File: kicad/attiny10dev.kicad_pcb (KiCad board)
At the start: 2 copper layers, 19 parts, among them J1 Conn_02x06_Odd_Even, J2 Conn_01x06, J3 Conn_01x03_Male, K1 m4-12h, K2 m4-12h, Q1 2N7002, Q2 BSS84, Q3 2N7002, Q4 FZT600, Q5 2N7002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

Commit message: Work on next gen pcb
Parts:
- added C10: 100n, Capacitor_SMD:C_0805_2012Metric_Pad1.15x1.40mm_HandSolder, F.Cu at (239.3, 85.1)
- added C11: 500p, Capacitor_SMD:C_0805_2012Metric_Pad1.15x1.40mm_HandSolder, F.Cu at (259.4, 81.6)
- added C12: 470u, Capacitor_THT:CP_Radial_D8.0mm_P5.00mm, F.Cu at (254.3, 105.8)
- added C4: 1u, Capacitor_SMD:C_0805_2012Metric_Pad1.15x1.40mm_HandSolder, F.Cu at (233.8, 92.5)
- added C5: 100n, Capacitor_SMD:C_0805_2012Metric_Pad1.15x1.40mm_HandSolder, F.Cu at (243.7, 67.6)
- added C6: 100n, Capacitor_SMD:C_0805_2012Metric_Pad1.15x1.40mm_HandSolder, F.Cu at (250.8, 96.8)
- added C7: 100n, Capacitor_SMD:C_0805_2012Metric_Pad1.15x1.40mm_HandSolder, F.Cu at (246.6, 85.2)
- added C8: 100n, Capacitor_SMD:C_0805_2012Metric_Pad1.15x1.40mm_HandSolder, F.Cu at (237.6, 101.1)
- added C9: 470u, Capacitor_THT:CP_Radial_D8.0mm_P5.00mm, F.Cu at (263.6, 105.8)
- added D2: D, Diode_SMD:D_3220_8050Metric_Pad2.65x5.15mm_HandSolder, F.Cu at (259.5, 89.8)
- added F1: 500ma, Fuse:Fuse_1206_3216Metric_Pad1.42x1.75mm_HandSolder, F.Cu at (231.2, 95.9)
- added L1: 33u, Inductor_THT:L_Toroid_Vertical_L13.0mm_W6.5mm_P5.60mm, F.Cu at (272.8, 91.5)
- added R10: 10k, Capacitor_SMD:C_0603_1608Metric_Pad1.05x0.95mm_HandSolder, F.Cu at (254.2, 97.8)
- added R4: 10k, Capacitor_SMD:C_0603_1608Metric_Pad1.05x0.95mm_HandSolder, F.Cu at (217.7, 105.5)
- added R5: 22, Capacitor_SMD:C_0603_1608Metric_Pad1.05x0.95mm_HandSolder, F.Cu at (229.6, 90.7)
- added R6: 22, Capacitor_SMD:C_0603_1608Metric_Pad1.05x0.95mm_HandSolder, F.Cu at (229.6, 89.0)
- added R7: 470m, Resistor_THT:R_Axial_DIN0204_L3.6mm_D1.6mm_P2.54mm_Vertical, F.Cu at (258.3, 97.6)
- added R8: 180, Capacitor_SMD:C_0603_1608Metric_Pad1.05x0.95mm_HandSolder, F.Cu at (263.8, 98.6)
- added R9: 86k, Capacitor_SMD:C_0603_1608Metric_Pad1.05x0.95mm_HandSolder, F.Cu at (256.0, 97.8)
- added SW1: SW_Push, Button_Switch_THT:SW_PUSH_6mm, F.Cu at (220.2, 101.5)
- added U3: ATmega32U4-AU, Package_QFP:TQFP-44_10x10mm_P0.8mm, F.Cu at (243.0, 93.0)
- added U4: MC34063AD, Package_DIP:DIP-8_W10.16mm, F.Cu at (263.3, 84.7)
- added Y1: 16Mhz, Crystal:Crystal_SMD_HC49-SD, F.Cu at (242.9, 104.9)
- C2, C3: value 22u -> 22p; footprint Capacitor_THT:CP_Radial_D12.5mm_P5.00mm -> Capacitor_SMD:C_0805_2012Metric_Pad1.15x1.40mm_HandSolder; moved to F.Cu
- D1, J1, K1, K2, U2: moved to F.Cu
- J2: value Conn_01x06 -> Conn_02x03_Odd_Even; footprint Connector_PinHeader_2.54mm:PinHeader_1x06_P2.54mm_Vertical -> Connector_PinHeader_2.54mm:PinHeader_2x03_P2.54mm_Vertical; moved to F.Cu
- J3: value Conn_01x03_Male -> USB_B; footprint TerminalBlock_RND:TerminalBlock_RND_205-00277_1x03_P5.00mm_Vertical -> Connector_USB:USB_B_OST_USB-B1HSxx_Horizontal; moved to F.Cu
- Q4: value FZT600 -> 2N7002; footprint Package_TO_SOT_THT:TO-92 -> Package_TO_SOT_SMD:SOT-23; moved to F.Cu
- R1, R2, R3: footprint Resistor_SMD:R_0805_2012Metric_Pad1.15x1.40mm_HandSolder -> Capacitor_SMD:C_0603_1608Metric_Pad1.05x0.95mm_HandSolder
- moved K2 216.4 mm to (268.6, 69.3), turned to 0 degrees
- moved J2 194.5 mm to (231.1, 100.2)
- moved C3 193.4 mm to (241.1, 101.1)
- moved Q5 192.8 mm to (232.0, 80.2), turned to 90 degrees
- moved K1 191.9 mm to (256.2, 69.9), turned to 0 degrees
- moved R1 190.4 mm to (229.3, 76.4), turned to 270 degrees
- moved R3 188.3 mm to (232.2, 77.0), turned to 180 degrees
- moved Q1 185.6 mm to (223.8, 80.3), turned to 90 degrees
- moved Q3 185.5 mm to (228.0, 80.3), turned to 0 degrees
- moved Q2 183.8 mm to (226.2, 76.5), turned to 180 degrees
- moved C1 179.5 mm to (259.3, 100.1), turned to 0 degrees
- moved D1 175.2 mm to (231.6, 74.7), turned to 0 degrees
- moved C2 175.2 mm to (244.6, 101.1)
- moved Q4 171.3 mm to (236.1, 78.2), turned to 90 degrees
- moved J3 168.1 mm to (224.8, 92.2), turned to 180 degrees
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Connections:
- C2 pad 1: GND -> Net-(C2-Pad1)
- C2 pad 2: +5V -> GND
- C3 pad 1: GND -> Net-(C3-Pad1)
- C3 pad 2: +12V -> GND
- J2 pad 1: /tpidata -> /prog_miso
- J2 pad 2: /tpiclk -> +5V
- J2 pad 3: /prog -> /prog_sck
- J2 pad 4: /hard_reset -> /prog_mosi
- J2 pad 5: /reset_low -> /prog_rst
- J3 pad 1: +12V -> Net-(F1-Pad1)
- J3 pad 2: GND -> Net-(J3-Pad2)
- J3 pad 3: +5V -> Net-(J3-Pad3)
- K1 pad 1: /lower_relay -> +12V
- K1 pad 10: +12V -> /lower_relay
- K1 pad 5: /tpiclk -> /tpi_clk
- K1 pad 6: /tpidata -> /tpi_data
- Q4 pad 1: GND -> /prog
- Q4 pad 2: Net-(Q4-Pad2) -> GND
- R2 pad 1: Net-(Q4-Pad2) -> /prog
- R2 pad 2: /prog -> GND
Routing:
- net /io3: track 58.3 -> 0.00 mm
- net +12V: track 55.2 -> 0.00 mm
- net /pb3: track 45.2 -> 0.00 mm
- net +5V: track 100.4 -> 55.7 mm, vias 1 -> 0
- net Net-(K2-Pad5): track 44.1 -> 0.00 mm, vias 2 -> 0
- net /prog: track 40.7 -> 0.00 mm
- net /pb1: track 35.6 -> 0.00 mm
- net /io0: track 34.9 -> 0.00 mm
- net /pb0: track 33.3 -> 0.00 mm
- net /lower_relay: track 31.7 -> 0.00 mm
- net /tpiclk: track 31.0 -> 0.00 mm
- net /io1: track 26.2 -> 0.00 mm
- net /hard_reset: track 25.9 -> 0.00 mm
- net /tpidata: track 23.2 -> 0.00 mm
- net /reset_low: track 18.6 -> 0.00 mm
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- removed copper zone on B.Cu, net GND
- removed copper zone on F.Cu, net GND
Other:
- net class Default: via_dia 1.5 -> 0.8
- board text removed: "."
- board text removed: "ATtiny10 V4"
- board text removed: "Anton Lööf"
- board text removed: "gnd +5 io3 io2 io1 io0"
- board text removed: "gnd rst0 rst1 prog tclk tdat"

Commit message: V2 of pcb
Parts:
- moved J1 93.4 mm to (149.7, 99.5), turned to 180 degrees
- moved U1 91.4 mm to (157.2, 89.4), turned to 90 degrees
- moved U2 83.4 mm to (161.5, 93.5), turned to 90 degrees
- moved C5 82.8 mm to (163.9, 89.7), turned to 270 degrees
- moved K2 82.7 mm to (187.2, 84.1), turned to 90 degrees
- moved R10 80.2 mm to (178.0, 122.8)
- moved R9 80.2 mm to (179.8, 122.7)
- moved C11 79.3 mm to (184.5, 107.4)
- moved C1 79.1 mm to (184.3, 125.2)
- moved L1 79.1 mm to (197.8, 116.5)
- moved R7 79.1 mm to (183.3, 122.7)
- moved U4 79.1 mm to (188.3, 109.7)
- moved D2 79.1 mm to (184.5, 114.8)
- moved R8 79.1 mm to (188.8, 123.7)
- moved C10 78.9 mm to (163.8, 107.8)
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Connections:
- K1 pad 3: /pb1 -> /pb0
- K1 pad 4: /io1 -> /io0
- K1 pad 5: /tpi_clk -> /tpi_data
- K1 pad 6: /tpi_data -> /tpi_clk
- K1 pad 7: /io0 -> /io1
- K1 pad 8: /pb0 -> /pb1
- U3 pad 37: /prog -> /tpi_clk
- U3 pad 38: /tpi_clk -> /tpi_data
- U3 pad 39: /tpi_data -> /prog
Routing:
- net +5V: track 55.7 -> 190.2 mm, vias 0 -> 2
- net /lower_relay: track 0.00 -> 68.8 mm
- net +12V: track 0.00 -> 66.5 mm, vias 0 -> 2
- net /io1: track 0.00 -> 54.0 mm
- net /io3: track 0.00 -> 51.0 mm
- net /io0: track 0.00 -> 48.6 mm
- net Net-(K2-Pad5): track 0.00 -> 45.8 mm
- net /tpi_clk: track 0.00 -> 43.6 mm
- net /pb3: track 0.00 -> 36.1 mm
- net /pb0: track 0.00 -> 36.0 mm
- net /io2: track 0.00 -> 33.9 mm
- net /tpi_data: track 0.00 -> 33.8 mm
- net /pb1: track 0.00 -> 33.0 mm
- net GND: track 24.4 -> 39.9 mm, vias 0 -> 8
- net /prog_rst: track 18.3 -> 32.1 mm
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- added copper zone on B.Cu, net GND
- added copper zone on F.Cu, net GND

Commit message: Finalize rev 2 pcb
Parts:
- added +12: TestPoint, TestPoint:TestPoint_THTPad_D1.0mm_Drill0.5mm, F.Cu at (170.8, 80.0)
- added pb0: TestPoint, TestPoint:TestPoint_THTPad_D1.0mm_Drill0.5mm, F.Cu at (163.0, 80.0)
- added pb1: TestPoint, TestPoint:TestPoint_THTPad_D1.0mm_Drill0.5mm, F.Cu at (167.0, 80.0)
- added pb2: TestPoint, TestPoint:TestPoint_THTPad_D1.0mm_Drill0.5mm, F.Cu at (159.0, 80.0)
- added pb3: TestPoint, TestPoint:TestPoint_THTPad_D1.0mm_Drill0.5mm, F.Cu at (155.0, 80.0)
- moved J1 2.80 mm to (152.5, 99.4)
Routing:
- net /pb0: track 36.0 -> 54.8 mm
- net /pb1: track 33.0 -> 48.6 mm
- net +12V: track 66.5 -> 78.1 mm
- net /pb3: track 36.1 -> 45.0 mm
- net +5V: track 190.2 -> 182.1 mm
- net /io2: track 33.9 -> 41.0 mm
- net /io0: track 48.6 -> 46.1 mm
- net /io1: track 54.0 -> 51.9 mm
- net /io3: track 51.0 -> 49.8 mm
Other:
- board outline added: 62 x 57 mm
- board text added: "AtTiny10prog Anton Lööf V2"
- board text added: "GND +5 io3 io2 io1 io0"

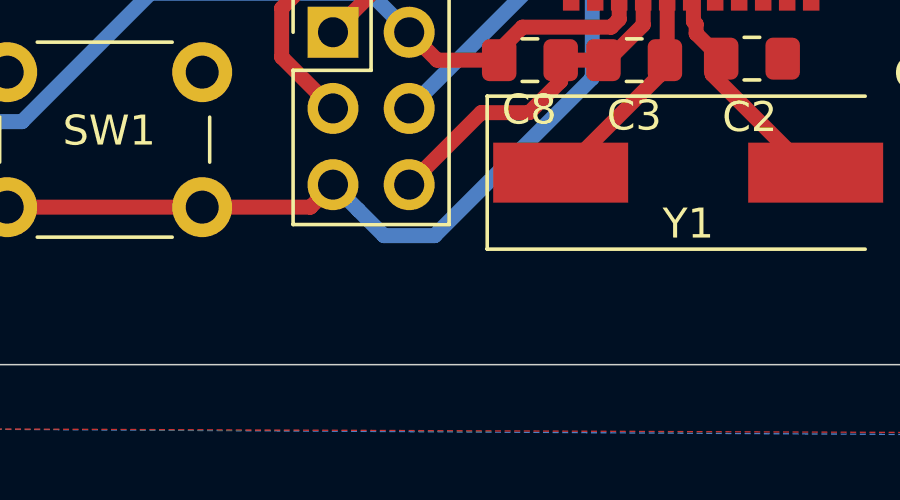
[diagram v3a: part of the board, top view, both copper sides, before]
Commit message: add jlc order no marker
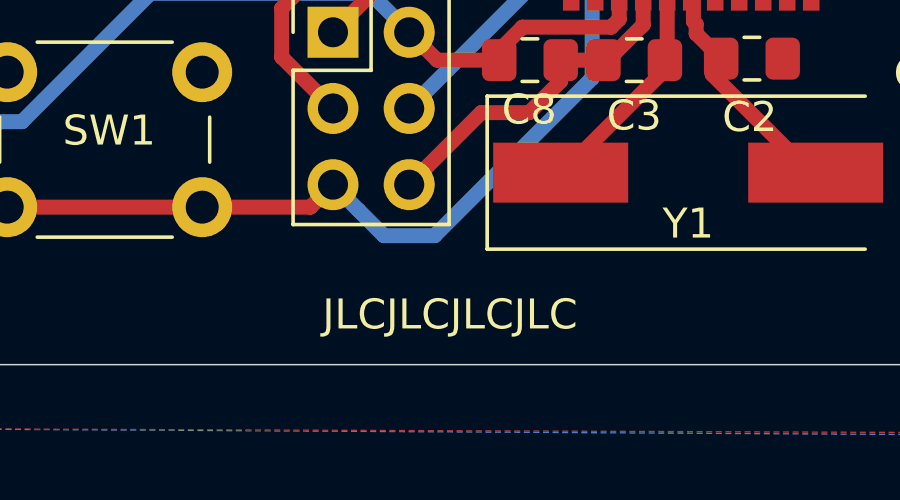
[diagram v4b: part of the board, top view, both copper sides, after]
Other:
- board text added: "JLCJLCJLCJLC"
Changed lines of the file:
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@@
   (general
     (thickness 1.6)
-    (drawings 6)
+    (drawings 7)
     (tracks 375)
     (zones 0)
@@
   )
   (setup
-    (last_trace_width 1)
+    (last_trace_width 0.5)
     (user_trace_width 1)
     (trace_clearance 0.2)
@@
       (net 11 /pb3))
   )
+  (gr_text JLCJLCJLCJLC (at 159.46 132.33) (layer F.SilkS)
+    (effects (font (size 1 1) (thickness 0.2)))
+  )
   (gr_text "AtTiny10prog\nAnton Lööf V2" (at 142.8 81.4) (layer F.SilkS)
